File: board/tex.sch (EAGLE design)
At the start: 271 parts, among them Q1 IRFZ44, Q10 FDD4141, Q11 2N7002, Q12 2N7002, Q13 2N7002, Q14 2N7002, Q15 2N7002, Q16 2N7002, Q17 2N7002, Q18 2N7002, Q19 2N7002, Q2 IRFZ44, Q20 2N7002, Q21 FDD4141, Q22 FDD4141, Q23 FDD4141, Q24 FDD4141, Q25 FDD4141, Q26 FDD4141, Q27 FDD4141, Q28 FDD4141, Q29 FDD4141, Q3 IRFZ44, Q30 FDD4141, Q31 2N7002, Q32 2N7002, Q33 2N7002, Q34 2N7002, Q35 2N7002, Q36 2N7002, Q37 2N7002, Q38 2N7002, Q39 2N7002, Q4 IRFZ44, Q40 2N7002, Q41 FDD4141, Q42 2N7002, Q43 2N7002, Q44 2N7002, Q45 2N7002, Q46 2N7002, Q47 2N7002, Q5 FDD4141, Q6 FDD4141, Q7 FDD4141, Q8 FDD4141, Q9 FDD4141, U1 RELAY-S108T02PTH, U12 OPTO-LTV817, U13 OPTO-LTV817, U14 OPTO-LTV817, U15 OPTO-LTV817, U17 24LC32A, U18 IO-HC4051, U2 RELAY-S108T02PTH, U4 AZ23C5V1, Y1 32.768KHz

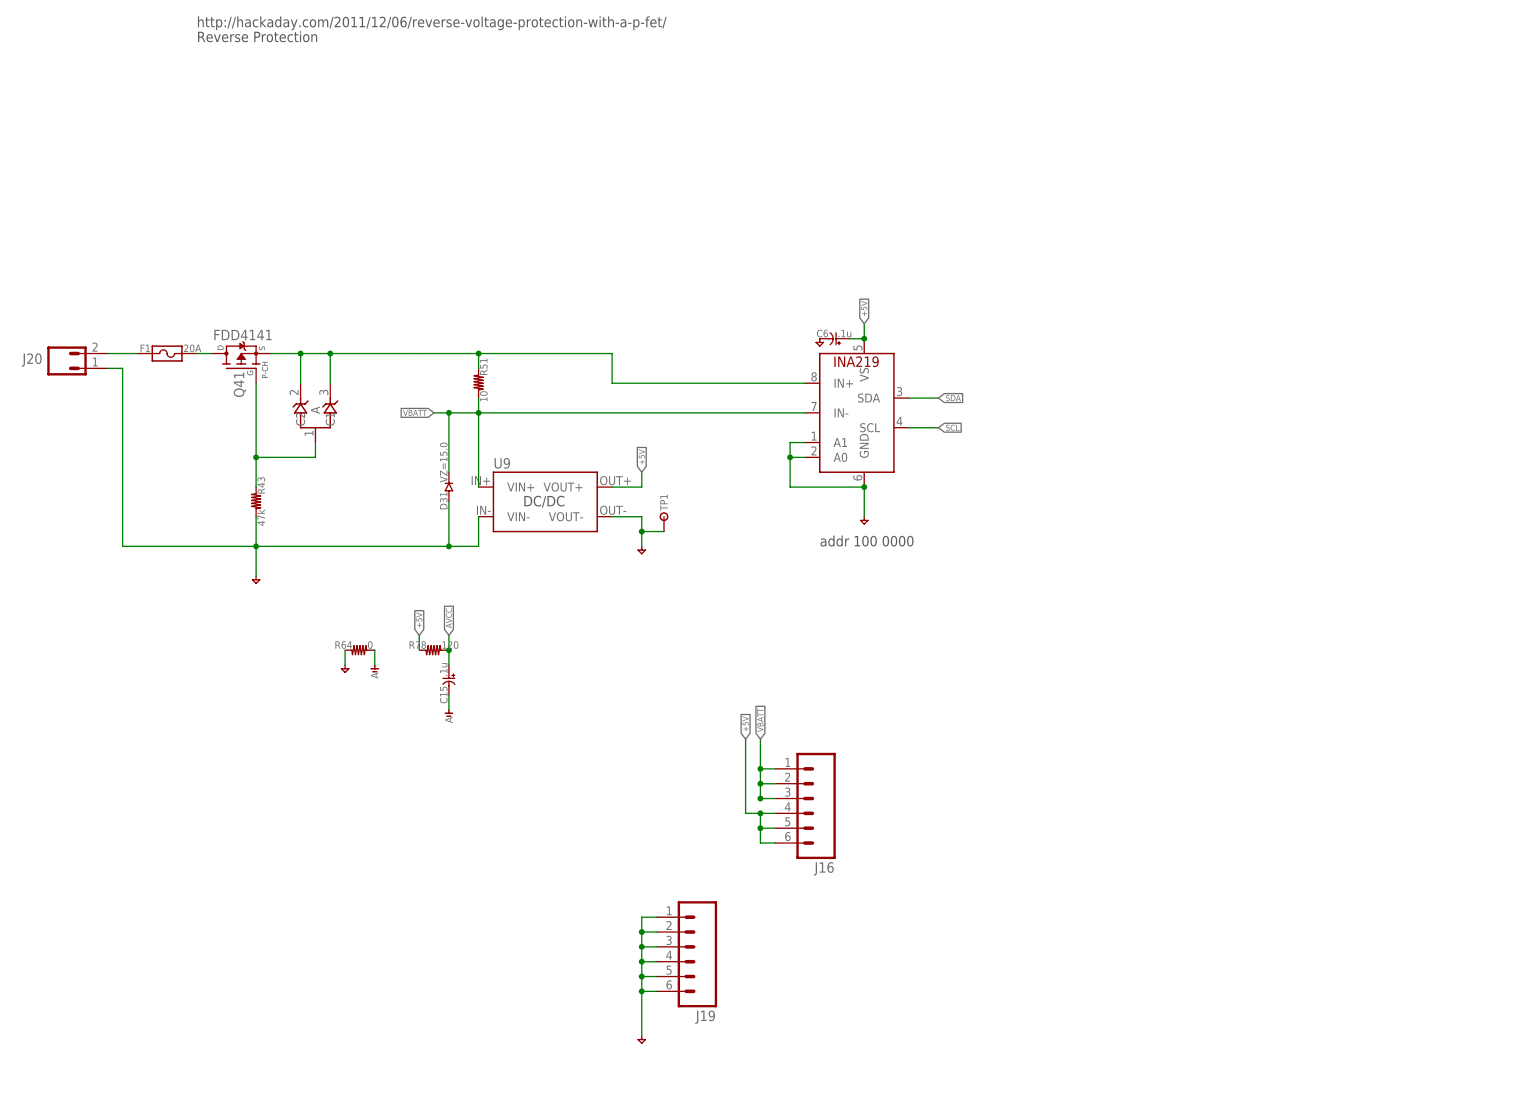
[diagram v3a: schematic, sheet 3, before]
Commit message: added descriptions to all circuit elements, generated update schematic
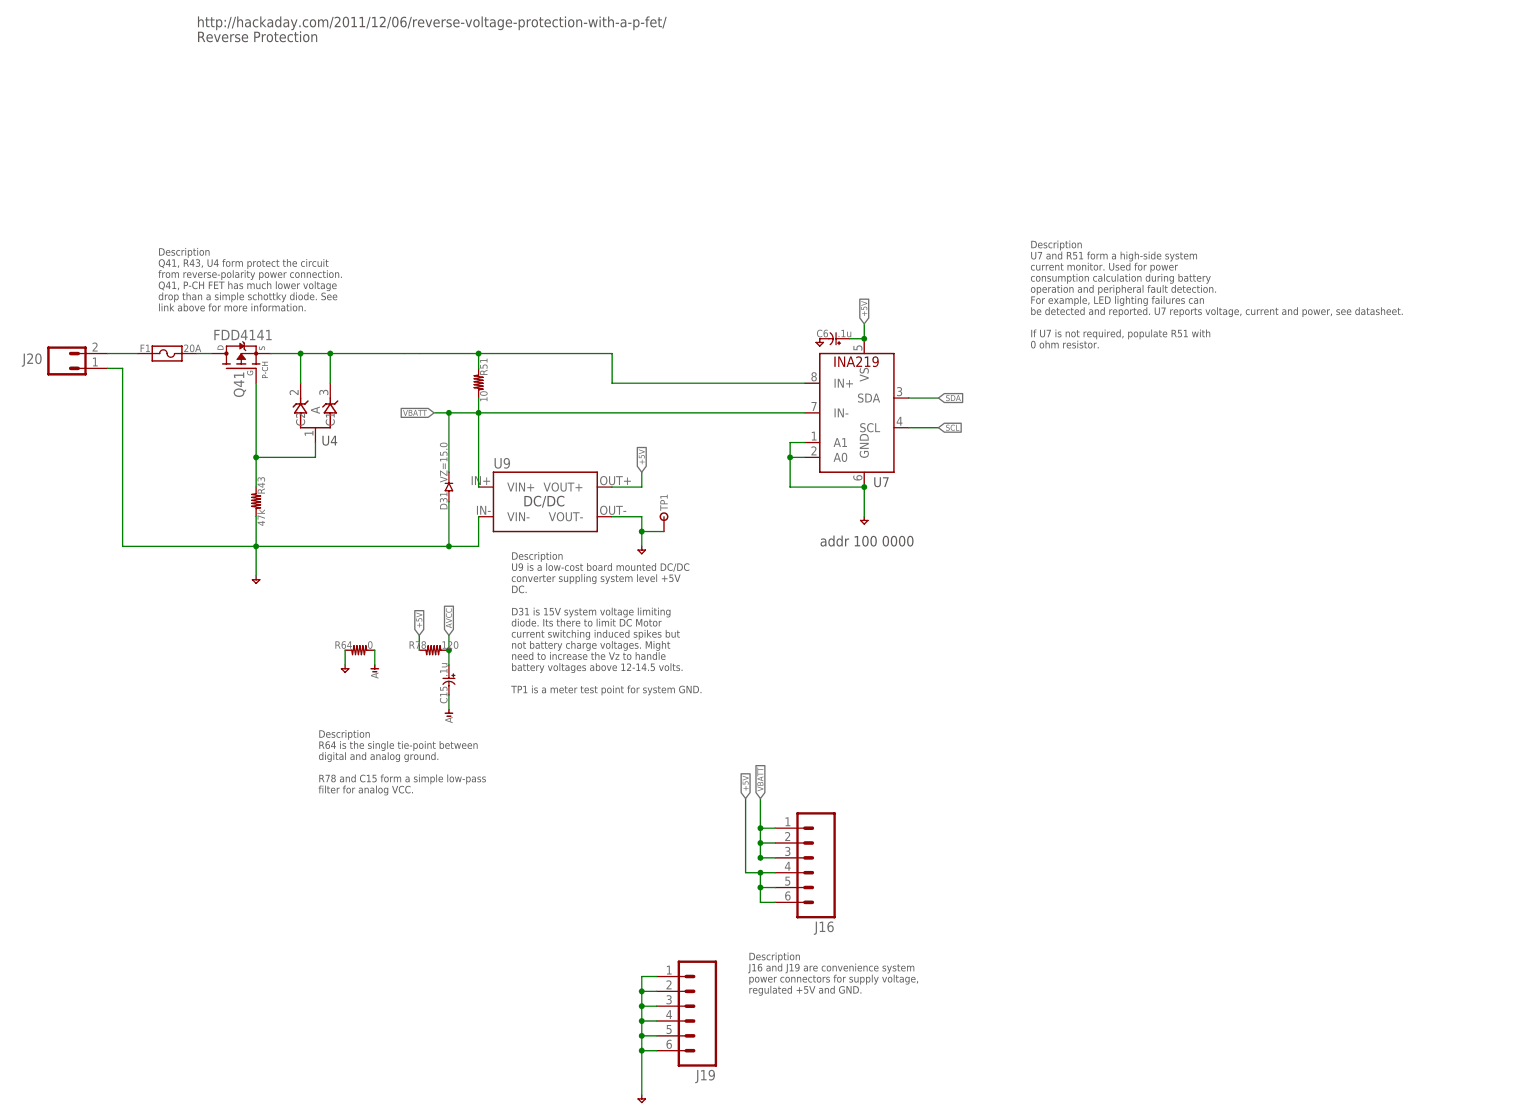
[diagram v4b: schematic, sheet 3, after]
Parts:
- removed K5: (no value), holla:RELAY-SPST-19X15X15MM
- U1, U2: value RELAY-S108T02PTH -> (none)
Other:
- note added: "Description For H-bridge operation (DC Motor), populate D17-D20 instead of D1-D4. D17-D20 indicate H-bridge output direction."
- note added: "Description HATs that follow RPi interface guidelines contain an on-board EEPROM used during linux startup hardware discovery phase. It is optional."
- note added: "Description J14, J15, U12-U14 provide 4 channels of optically isolated inputs connected directly to RPi input pins. These are labeled and DC motor encoder A-B inputs but they are general purpose inputs. R65-R68 need to current-limit opto input to less that 30mA if LTV817 is used."
- note added: "Description J16 and J19 are convenience system power connectors for supply voltage, regulated +5V and GND."
- note added: "Description J17 and J18 are labeled for external stepper-motor driver operation. However, J17 and J18 circuitry each offers direct RPi output pin controlled 3 channel general purpose open-drain signals. The output current is limited by device selected for Q42-Q47."
- note added: "Description J29 is a convenience connector for external switches. Connect switch to J29 and GND, requires U16 input pin pull-up resistor configuration. See datasheet."
- note added: "Description J30 is a convenience connector suppling +5V, 4 I/O pins and GND. Pins configured for input can have interrupt on change if configured. See U16 datasheet."
- note added: "Description K1-K4 are general purpose relays permitting both normally-open and normally-closed connections. Voltage and current maximum are relay dependent."
- note added: "Description Q41, R43, U4 form protect the circuit from reverse-polarity power connection. Q41, P-CH FET has much lower voltage drop than a simple schottky diode. See link above for more information."
- note added: "Description R64 is the single tie-point between digital and analog ground. R78 and C15 form a simple low-pass filter for analog VCC."
- note added: "Description The Tex Hat is a multi-purpose expansion board. This page is overall block diagram. Each page contains brief descriptions outlining individual functionality. The board does not require full component population to function. System designers can pick and choose what capabilities required. Also, see "use cases.ods" for additional functionally descriptions."
- note added: "Description These switches and LEDs are directly connected to RPi I/O for simplicity. During development these can be used for debugging, during operation they offer a local front panel interface."
- note added: "Description This page contains 8-channel external analog-voltage sense circuitry, J21-J28. Each voltage is conditioned and feed to an 8-to-1 analog demultiplexer, U18. RPi makes channel selection via SENSORS0-SENSORS2 using direct I/O pins. U18 output voltage is buffered through U11A and voltage divider R58 and R59. U10, an I2C ADC is configured for single-ended ground referenced inputs, 1 for U1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"
- note added: "Description U1 and U2 are board mounted solid-state relays, SSR. Originally designed for Sharp S108T2 SSR, which is no-longer available. IXYS CPC1998 can be used with slight pin bending. Remember, SSRs are for AC line switching."
- note added: "Description U16 is a 16-bit I2C power expander. Port A0-5 outputs enables for relay drivers for U1, U2, and K1-K4. U16 can be configured to send interrupt single to RPi on input pin change. See datasheet for more information."
- note added: "Description U19 is a battery-backed real time clock for offline RPi operation where NTP is not available."
- note added: "Description U20 isn't an IC but a connector for a display module, can be LCD or OLED. CAUTION: verify display pinout before plugging in display. Display pinouts are not standardized. Use J11 for harness connection if required or for other additionalexternal I2C devices."
- note added: "Description U3 is a full-duplex differential line driver connected to UART0 commonly used for RS-485 and RS-422 inter-board serial communication."
- note added: "Description U5 is a 16-channel I2C PWM generator. It combined with the top row of P-CH FETs form 16 battery- power modulation circuits, i.e. for 12V LED intensity control. Channels 12-15 offer an additional functionality, 2 full H-Bridges for DC motor speed and direction control. R33 and R34 are motor current sense resistors for monitoring, fault detection and reporting. If motor control isn't a 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"
- note added: "Description U6A-B are gain/filter stages for DC MOTORA and MOTORB powered by PWM-enabled H-Bridges on sheet 5. Their output is feed into U10 ADC on sheet 6."
- note added: "Description U7 and R51 form a high-side system current monitor. Used for power consumption calculation during battery operation and peripheral fault detection. For example, LED lighting failures can be detected and reported. U7 reports voltage, current and power, see datasheet. If U7 is not required, populate R51 with 0 ohm resistor."
- note added: "Description U8 is an I2C digital temperature sensor to monitor board-level temperature."
- note added: "Description U9 is a low-cost board mounted DC/DC converter suppling system level +5V DC. D31 is 15V system voltage limiting diode. Its there to limit DC Motor current switching induced spikes but not battery charge voltages. Might need to increase the Vz to handle battery voltages above 12-14.5 volts. TP1 is a meter test point for system GND."
- note added: "U4"
- note added: "U7"
- note added: "v0.1 CH"
- note removed: "ToDo List"
- moved on the sheet: D19, D20, J16, J19

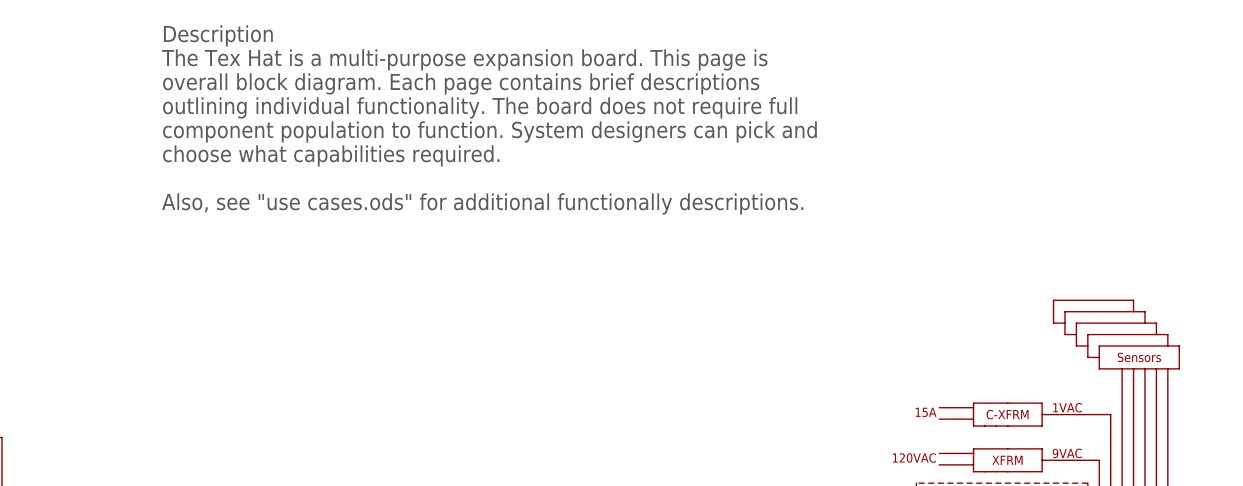
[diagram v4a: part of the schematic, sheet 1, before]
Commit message: added part number
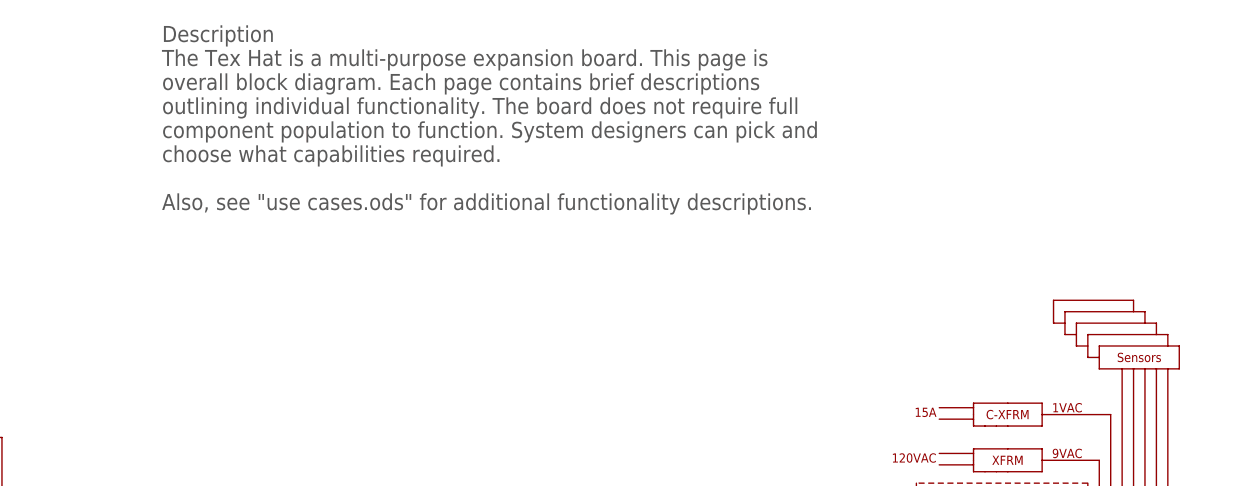
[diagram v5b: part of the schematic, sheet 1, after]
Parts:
- U10: value (none) -> ADS1x15
- U11, U6: value (none) -> DUALOPAMP
- U16: value (none) -> MCP23017
- U19: value (none) -> MCP7940N
- U3: value (none) -> MAX13433E
- U5: value (none) -> PCA9685
- U7: value (none) -> INA219
- U8: value (none) -> LM75
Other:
- note added: "Description The Tex Hat is a multi-purpose expansion board. This page is overall block diagram. Each page contains brief descriptions outlining individual functionality. The board does not require full component population to function. System designers can pick and choose what capabilities required. Also, see "use cases.ods" for additional functionality descriptions."
- note added: "Description U16 is a 16-bit I2C port expander. Port A0-5 outputs enables for relay drivers for U1, U2, and K1-K4. U16 can be configured to send interrupt single to RPi on input pin change. See datasheet for more information."
- note removed: "Description The Tex Hat is a multi-purpose expansion board. This page is overall block diagram. Each page contains brief descriptions outlining individual functionality. The board does not require full component population to function. System designers can pick and choose what capabilities required. Also, see "use cases.ods" for additional functionally descriptions."
- note removed: "Description U16 is a 16-bit I2C power expander. Port A0-5 outputs enables for relay drivers for U1, U2, and K1-K4. U16 can be configured to send interrupt single to RPi on input pin change. See datasheet for more information."
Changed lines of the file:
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@@
 <part name="Y1" library="holla" deviceset="CRYSTAL32-SMD" device="ABS25" value="32.768KHz"/>
 <part name="GND5" library="holla" deviceset="GND" device=""/>
-<part name="U10" library="holla" deviceset="ADC-ADS1015" device="-MSOP10"/>
-<part name="U8" library="holla" deviceset="SENSOR-TEMP-LM75" device="-SO08"/>
+<part name="U10" library="holla" deviceset="ADC-ADS1015" device="-MSOP10" value="ADS1x15"/>
+<part name="U8" library="holla" deviceset="SENSOR-TEMP-LM75" device="-SO08" value="LM75"/>
 <part name="GND6" library="holla" deviceset="GND" device=""/>
 <part name="C8" library="holla" deviceset="C" device="-0603" value=".1u"/>
@@
 <part name="R62" library="holla" deviceset="R" device="-0603" value="220"/>
 <part name="FRAME5" library="holla" deviceset="FRAME_A_L" device="" value="LED"/>
-<part name="U5" library="holla" deviceset="IO-PCA9685" device="-TSSOP28"/>
+<part name="U5" library="holla" deviceset="IO-PCA9685" device="-TSSOP28" value="PCA9685"/>
 <part name="C2" library="holla" deviceset="C" device="-0603" value=".1u"/>
 <part name="GND46" library="holla" deviceset="GND" device=""/>
@@
 <part name="R44" library="holla" deviceset="R" device="-0603" value="1k"/>
 <part name="R55" library="holla" deviceset="R" device="-0603" value="1k"/>
-<part name="U6" library="holla" deviceset="AMP-OPAMP-DUAL" device="-SO08"/>
+<part name="U6" library="holla" deviceset="AMP-OPAMP-DUAL" device="-SO08" value="DUALOPAMP"/>
 <part name="R53" library="holla" deviceset="R" device="-0603" value="10k"/>
 <part name="R56" library="holla" deviceset="R" device="-0603" value="1k"/>
@@
 <part name="R28" library="holla" deviceset="R" device="-0603" value="DNP"/>
 <part name="R19" library="holla" deviceset="R" device="-0603" value="0"/>
-<part name="U16" library="holla" deviceset="IO-MCP23017" device="SO"/>
+<part name="U16" library="holla" deviceset="IO-MCP23017" device="SO" value="MCP23017"/>
 <part name="GND20" library="holla" deviceset="GND" device=""/>
 <part name="J29" library="holla" deviceset="CONN-06" device="-PLUGIN-SCREW"/>
@@
 <part name="R86" library="holla" deviceset="R" device="-0603" value="47k"/>
 <part name="R87" library="holla" deviceset="R" device="-0603" value="10k"/>
-<part name="U7" library="holla" deviceset="ADC-INA219" device="-SOIC8"/>
+<part name="U7" library="holla" deviceset="ADC-INA219" device="-SOIC8" value="INA219"/>
 <part name="U4" library="brightleaf" deviceset="AZ23CXXX" device="" value="AZ23C5V1"/>
 <part name="Q41" library="brightleaf" deviceset="FDD4141" device="TO252" value="FDD4141"/>
@@
 <part name="R91" library="holla" deviceset="R" device="-0603" value="10k"/>
 <part name="U20" library="holla" deviceset="DISP-I2C-4PIN" device=""/>
-<part name="U3" library="holla" deviceset="COMM-MAX13433E" device=""/>
+<part name="U3" library="holla" deviceset="COMM-MAX13433E" device="" value="MAX13433E"/>
 <part name="J13" library="holla" deviceset="CONN-05" device="-PLUGIN-SCREW"/>
 <part name="J12" library="holla" deviceset="CONN-02" device="-0.1"/>
@@
 <part name="R72" library="holla" deviceset="R" device="-0603" value="1k"/>
 <part name="R71" library="holla" deviceset="R" device="-0603" value="1k"/>
-<part name="U11" library="holla" deviceset="AMP-OPAMP-DUAL" device="-SO08"/>
+<part name="U11" library="holla" deviceset="AMP-OPAMP-DUAL" device="-SO08" value="DUALOPAMP"/>
 <part name="R63" library="holla" deviceset="R" device="-0603" value="0"/>
 <part name="R70" library="holla" deviceset="R" device="-0603" value="DNP"/>
@@
 <part name="R64" library="holla" deviceset="R" device="-0603" value="0"/>
 <part name="R43" library="holla" deviceset="R" device="-0603" value="47k"/>
-<part name="U19" library="holla" deviceset="RTC-MCP7940N" device=""/>
+<part name="U19" library="holla" deviceset="RTC-MCP7940N" device="" value="MCP7940N"/>
 <part name="R79" library="holla" deviceset="R" device="-0603" value="120"/>
 <part name="GND4" library="holla" deviceset="GND" device=""/>
@@
 component population to function. System designers can pick and
 choose what capabilities required.
-Also, see "use cases.ods" for additional functionally descriptions.</text>
+Also, see "use cases.ods" for additional functionality descriptions.</text>
 <text x="136.906" y="132.08" size="1.016" layer="94" rot="R180" align="center">ISENSE</text>
 <wire x1="140.97" y1="130.81" x2="135.89" y2="130.81" width="0.1524" layer="94"/>
@@
 install 0ohm resistor to select</text>
 <text x="43.688" y="171.704" size="1.27" layer="97" align="top-left">Description
-U16 is a 16-bit I2C power expander. Port
+U16 is a 16-bit I2C port expander. Port
 A0-5 outputs enables for relay drivers
 for U1, U2, and K1-K4.
